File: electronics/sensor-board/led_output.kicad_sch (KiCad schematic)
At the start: 0 parts

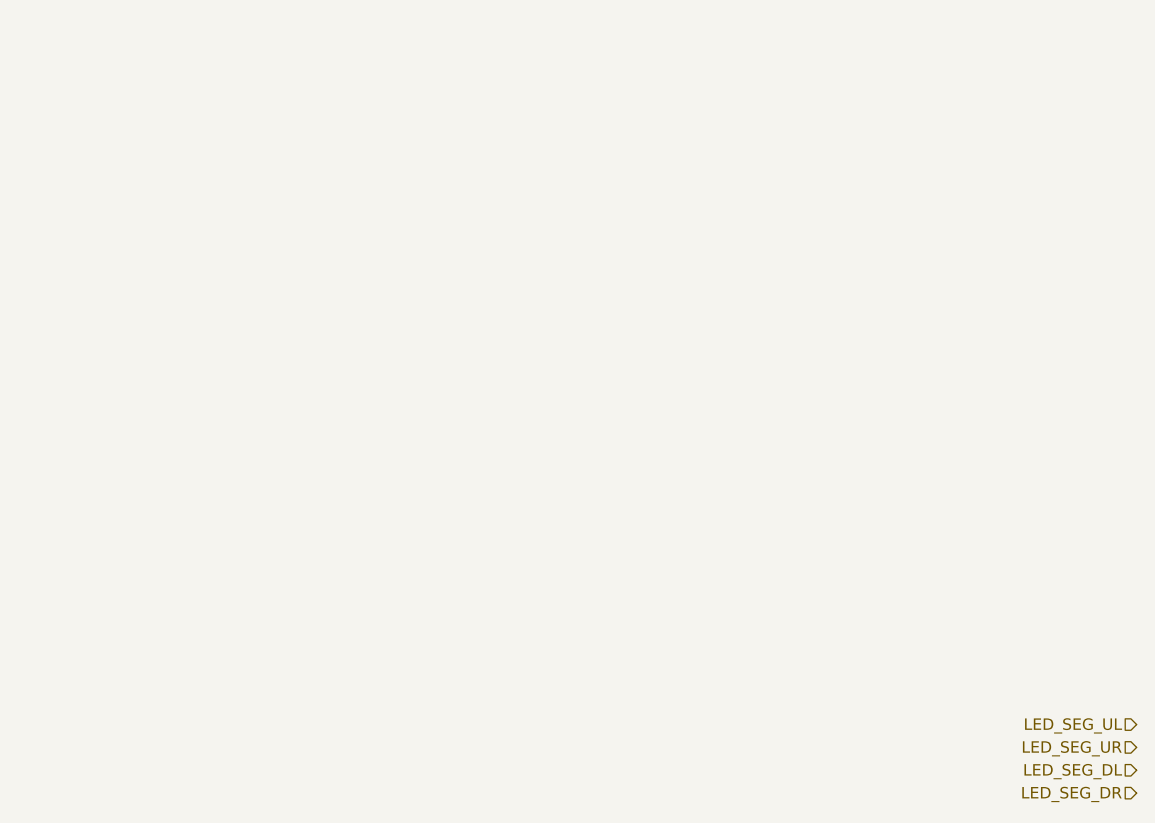
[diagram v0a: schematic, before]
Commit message: LED output, debug and minor controller changes
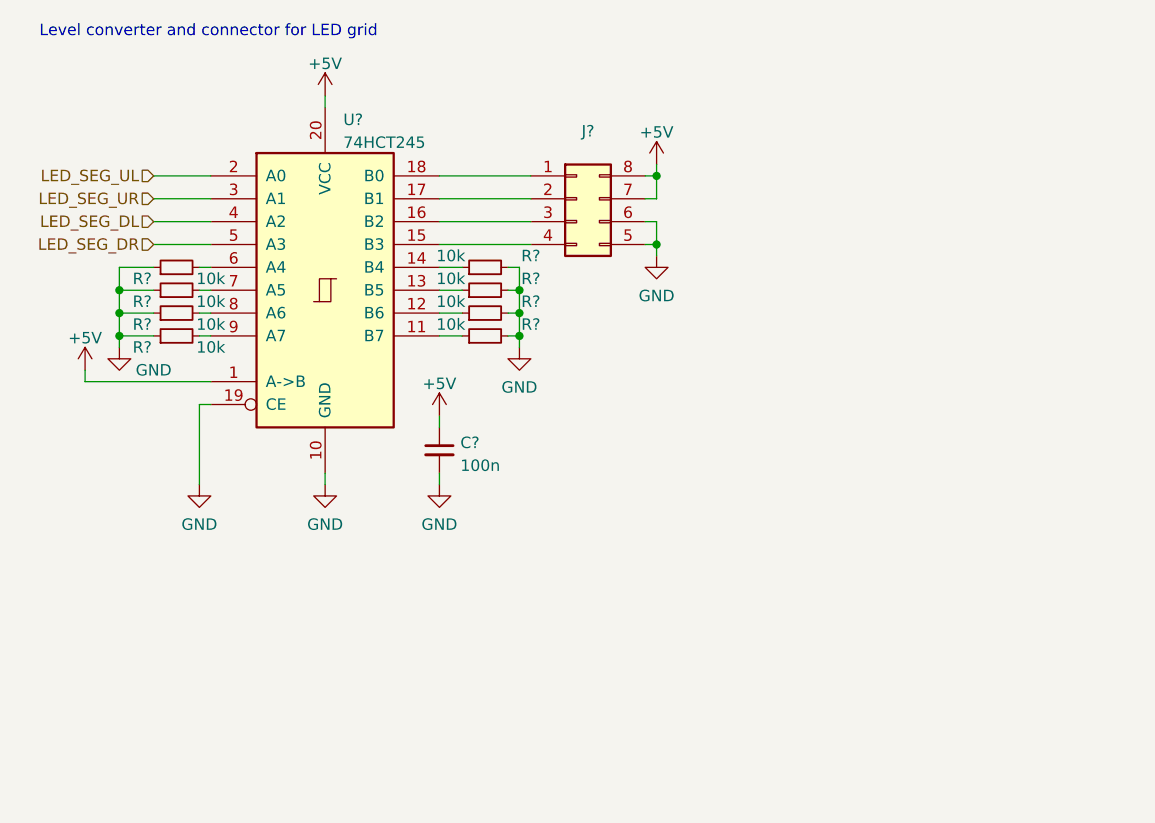
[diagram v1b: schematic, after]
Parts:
- added C?: 100n, symbol Device:C_Small
- added J?: Conn_02x04_Counter_Clockwise, symbol Connector_Generic:Conn_02x04_Counter_Clockwise
- added R? (x8): 10k, symbol Device:R_Small
- added U?: 74HCT245, symbol 74xx:74HC245
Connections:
- net LED_SEG_DL: now also U?.4 (A2)
- net LED_SEG_DR: now also U?.5 (A3)
- net LED_SEG_UL: now also U?.2 (A0)
- net LED_SEG_UR: now also U?.3 (A1)
- new net: R?.2, U?.6 (A4)
- new net: R?.1, U?.14 (B4)
- new net: R?.1, U?.12 (B6)
- new net: J?.1 (Pin_1), U?.18 (B0)
- new net: J?.2 (Pin_2), U?.17 (B1)
- new net: J?.3 (Pin_3), U?.16 (B2)
- new net: J?.4 (Pin_4), U?.15 (B3)
- new net: R?.1, U?.13 (B5)
- new net: R?.1, U?.11 (B7)
- new net: R?.2, U?.7 (A5)
- new net: R?.2, U?.8 (A6)
- new net: R?.2, U?.9 (A7)
- new net +5V: C?.1, J?.7 (Pin_7), J?.8 (Pin_8), U?.1 (A->B), U?.20 (VCC)
- new net GND: C?.2, J?.5 (Pin_5), J?.6 (Pin_6), R?.1, R?.1, R?.1, R?.1, R?.2, R?.2, R?.2, R?.2, U?.10 (GND), U?.19 (CE)
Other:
- note added: "Level converter and connector for LED grid"

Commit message: Build Pad Bus and annotate
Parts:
- gave numbers to parts that had none: 11
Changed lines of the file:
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@@
   (symbol (lib_id "Device:R_Small") (at 33.02 41.91 90) (unit 1)
     (in_bom yes) (on_board yes)
-    (property "Reference" "R?" (id 0) (at 29.21 43.18 90))
+    (property "Reference" "R59" (id 0) (at 29.21 43.18 90))
     (property "Value" "10k" (id 1) (at 36.83 43.18 90))
     (property "Footprint" "" (id 2) (at 33.02 41.91 0)
@@
   (symbol (lib_id "Device:R_Small") (at 67.31 41.91 90) (unit 1)
     (in_bom yes) (on_board yes)
-    (property "Reference" "R?" (id 0) (at 72.39 40.64 90))
+    (property "Reference" "R63" (id 0) (at 73.66 40.64 90))
     (property "Value" "10k" (id 1) (at 63.5 40.64 90))
     (property "Footprint" "" (id 2) (at 67.31 41.91 0)
@@
   (symbol (lib_id "power:GND") (at 49.53 66.04 0) (unit 1)
     (in_bom yes) (on_board yes) (fields_autoplaced)
-    (property "Reference" "#PWR?" (id 0) (at 49.53 72.39 0)
+    (property "Reference" "#PWR0108" (id 0) (at 49.53 72.39 0)
       (effects (font (size 1.27 1.27)) hide)
     )
@@
   (symbol (lib_id "power:GND") (at 62.23 66.04 0) (unit 1)
     (in_bom yes) (on_board yes) (fields_autoplaced)
-    (property "Reference" "#PWR?" (id 0) (at 62.23 72.39 0)
+    (property "Reference" "#PWR0110" (id 0) (at 62.23 72.39 0)
       (effects (font (size 1.27 1.27)) hide)
     )
@@
   (symbol (lib_id "Device:R_Small") (at 67.31 46.99 90) (unit 1)
     (in_bom yes) (on_board yes)
-    (property "Reference" "R?" (id 0) (at 72.39 45.72 90))
+    (property "Reference" "R65" (id 0) (at 73.66 45.72 90))
     (property "Value" "10k" (id 1) (at 63.5 45.72 90))
     (property "Footprint" "" (id 2) (at 67.31 46.99 0)
@@
   (symbol (lib_id "power:GND") (at 26.67 50.8 0) (unit 1)
     (in_bom yes) (on_board yes)
-    (property "Reference" "#PWR?" (id 0) (at 26.67 57.15 0)
+    (property "Reference" "#PWR0105" (id 0) (at 26.67 57.15 0)
       (effects (font (size 1.27 1.27)) hide)
     )
@@
   (symbol (lib_id "power:+5V") (at 62.23 58.42 0) (unit 1)
     (in_bom yes) (on_board yes) (fields_autoplaced)
-    (property "Reference" "#PWR?" (id 0) (at 62.23 62.23 0)
+    (property "Reference" "#PWR0109" (id 0) (at 62.23 62.23 0)
       (effects (font (size 1.27 1.27)) hide)
     )
@@
   (symbol (lib_id "power:GND") (at 71.12 50.8 0) (unit 1)
     (in_bom yes) (on_board yes) (fields_autoplaced)
-    (property "Reference" "#PWR?" (id 0) (at 71.12 57.15 0)
+    (property "Reference" "#PWR0111" (id 0) (at 71.12 57.15 0)
       (effects (font (size 1.27 1.27)) hide)
     )
@@
   (symbol (lib_id "power:+5V") (at 22.86 53.34 0) (unit 1)
     (in_bom yes) (on_board yes) (fields_autoplaced)
-    (property "Reference" "#PWR?" (id 0) (at 22.86 57.15 0)
+    (property "Reference" "#PWR0104" (id 0) (at 22.86 57.15 0)
       (effects (font (size 1.27 1.27)) hide)
     )
@@
   (symbol (lib_id "Connector_Generic:Conn_02x04_Counter_Clockwise") (at 77.47 34.29 0) (unit 1)
     (in_bom yes) (on_board yes) (fields_autoplaced)
-    (property "Reference" "J?" (id 0) (at 78.74 26.7802 0))
+    (property "Reference" "J19" (id 0) (at 78.74 26.7802 0))
     (property "Value" "Conn_02x04_Counter_Clockwise" (id 1) (at 78.74 29.3171 0)
       (effects (font (size 1.27 1.27)) hide)
@@
   (symbol (lib_id "Device:R_Small") (at 67.31 44.45 90) (unit 1)
     (in_bom yes) (on_board yes)
-    (property "Reference" "R?" (id 0) (at 72.39 43.18 90))
+    (property "Reference" "R64" (id 0) (at 73.66 43.18 90))
     (property "Value" "10k" (id 1) (at 63.5 43.18 90))
     (property "Footprint" "" (id 2) (at 67.31 44.45 0)
@@
   (symbol (lib_id "74xx:74HC245") (at 49.53 44.45 0) (unit 1)
     (in_bom yes) (on_board yes) (fields_autoplaced)
-    (property "Reference" "U?" (id 0) (at 51.5494 25.5102 0)
+    (property "Reference" "U11" (id 0) (at 51.5494 25.5102 0)
       (effects (font (size 1.27 1.27)) (justify left))
     )
@@
   (symbol (lib_id "Device:R_Small") (at 33.02 49.53 90) (unit 1)
     (in_bom yes) (on_board yes)
-    (property "Reference" "R?" (id 0) (at 29.21 50.8 90))
+    (property "Reference" "R62" (id 0) (at 29.21 50.8 90))
     (property "Value" "10k" (id 1) (at 36.83 50.8 90))
     (property "Footprint" "" (id 2) (at 33.02 49.53 0)
@@
   (symbol (lib_id "power:GND") (at 86.36 40.64 0) (unit 1)
     (in_bom yes) (on_board yes) (fields_autoplaced)
-    (property "Reference" "#PWR?" (id 0) (at 86.36 46.99 0)
+    (property "Reference" "#PWR0113" (id 0) (at 86.36 46.99 0)
       (effects (font (size 1.27 1.27)) hide)
     )
@@
   (symbol (lib_id "power:GND") (at 35.56 66.04 0) (unit 1)
     (in_bom yes) (on_board yes) (fields_autoplaced)
-    (property "Reference" "#PWR?" (id 0) (at 35.56 72.39 0)
+    (property "Reference" "#PWR0106" (id 0) (at 35.56 72.39 0)
       (effects (font (size 1.27 1.27)) hide)
     )
@@
   (symbol (lib_id "power:+5V") (at 49.53 22.86 0) (unit 1)
     (in_bom yes) (on_board yes) (fields_autoplaced)
-    (property "Reference" "#PWR?" (id 0) (at 49.53 26.67 0)
+    (property "Reference" "#PWR0107" (id 0) (at 49.53 26.67 0)
       (effects (font (size 1.27 1.27)) hide)
     )
@@
   (symbol (lib_id "Device:R_Small") (at 33.02 46.99 90) (unit 1)
     (in_bom yes) (on_board yes)
-    (property "Reference" "R?" (id 0) (at 29.21 48.26 90))
+    (property "Reference" "R61" (id 0) (at 29.21 48.26 90))
     (property "Value" "10k" (id 1) (at 36.83 48.26 90))
     (property "Footprint" "" (id 2) (at 33.02 46.99 0)
@@
   (symbol (lib_id "Device:R_Small") (at 67.31 49.53 90) (unit 1)
     (in_bom yes) (on_board yes)
-    (property "Reference" "R?" (id 0) (at 72.39 48.26 90))
+    (property "Reference" "R66" (id 0) (at 73.66 48.26 90))
     (property "Value" "10k" (id 1) (at 63.5 48.26 90))
     (property "Footprint" "" (id 2) (at 67.31 49.53 0)
@@
   (symbol (lib_id "Device:C_Small") (at 62.23 62.23 0) (unit 1)
     (in_bom yes) (on_board yes) (fields_autoplaced)
-    (property "Reference" "C?" (id 0) (at 64.5541 61.4016 0)
+    (property "Reference" "C46" (id 0) (at 64.5541 61.4016 0)
       (effects (font (size 1.27 1.27)) (justify left))
     )
@@
   (symbol (lib_id "Device:R_Small") (at 33.02 44.45 90) (unit 1)
     (in_bom yes) (on_board yes)
-    (property "Reference" "R?" (id 0) (at 29.21 45.72 90))
+    (property "Reference" "R60" (id 0) (at 29.21 45.72 90))
     (property "Value" "10k" (id 1) (at 36.83 45.72 90))
     (property "Footprint" "" (id 2) (at 33.02 44.45 0)
@@
   (symbol (lib_id "power:+5V") (at 86.36 30.48 0) (unit 1)
     (in_bom yes) (on_board yes) (fields_autoplaced)
-    (property "Reference" "#PWR?" (id 0) (at 86.36 34.29 0)
-      (effects (font (size 1.27 1.27)) hide)
-    )
+    (property "Reference" "#PWR0112" (id 0) (at 86.36 34.29 0)
+      (effects (font (size 1.27 1.27)) hide)
+    )

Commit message: Minor tweaks, footprints added
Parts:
- C46: footprint (none) -> Capacitor_SMD:C_0603_1608Metric
- J19: footprint (none) -> Connector_PinHeader_2.54mm:PinHeader_2x04_P2.54mm_Vertical
- R59, R60, R61, R62, R63, R64, R65, R66: footprint (none) -> Resistor_SMD:R_0603_1608Metric
- U11: footprint (none) -> Package_SO:TSSOP-20_4.4x6.5mm_P0.65mm
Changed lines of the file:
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@@
     (property "Reference" "R59" (id 0) (at 29.21 43.18 90))
     (property "Value" "10k" (id 1) (at 36.83 43.18 90))
-    (property "Footprint" "" (id 2) (at 33.02 41.91 0)
+    (property "Footprint" "Resistor_SMD:R_0603_1608Metric" (id 2) (at 33.02 41.91 0)
       (effects (font (size 1.27 1.27)) hide)
     )
@@
     (property "Reference" "R63" (id 0) (at 73.66 40.64 90))
     (property "Value" "10k" (id 1) (at 63.5 40.64 90))
-    (property "Footprint" "" (id 2) (at 67.31 41.91 0)
+    (property "Footprint" "Resistor_SMD:R_0603_1608Metric" (id 2) (at 67.31 41.91 0)
       (effects (font (size 1.27 1.27)) hide)
     )
@@
     (property "Reference" "R65" (id 0) (at 73.66 45.72 90))
     (property "Value" "10k" (id 1) (at 63.5 45.72 90))
-    (property "Footprint" "" (id 2) (at 67.31 46.99 0)
+    (property "Footprint" "Resistor_SMD:R_0603_1608Metric" (id 2) (at 67.31 46.99 0)
       (effects (font (size 1.27 1.27)) hide)
     )
@@
       (effects (font (size 1.27 1.27)) hide)
     )
-    (property "Footprint" "" (id 2) (at 77.47 34.29 0)
+    (property "Footprint" "Connector_PinHeader_2.54mm:PinHeader_2x04_P2.54mm_Vertical" (id 2) (at 77.47 34.29 0)
       (effects (font (size 1.27 1.27)) hide)
     )
@@
     (property "Reference" "R64" (id 0) (at 73.66 43.18 90))
     (property "Value" "10k" (id 1) (at 63.5 43.18 90))
-    (property "Footprint" "" (id 2) (at 67.31 44.45 0)
+    (property "Footprint" "Resistor_SMD:R_0603_1608Metric" (id 2) (at 67.31 44.45 0)
       (effects (font (size 1.27 1.27)) hide)
     )
@@
       (effects (font (size 1.27 1.27)) (justify left))
     )
-    (property "Footprint" "" (id 2) (at 49.53 44.45 0)
+    (property "Footprint" "Package_SO:TSSOP-20_4.4x6.5mm_P0.65mm" (id 2) (at 49.53 44.45 0)
       (effects (font (size 1.27 1.27)) hide)
     )
@@
     (property "Reference" "R62" (id 0) (at 29.21 50.8 90))
     (property "Value" "10k" (id 1) (at 36.83 50.8 90))
-    (property "Footprint" "" (id 2) (at 33.02 49.53 0)
+    (property "Footprint" "Resistor_SMD:R_0603_1608Metric" (id 2) (at 33.02 49.53 0)
       (effects (font (size 1.27 1.27)) hide)
     )
@@
     (property "Reference" "R61" (id 0) (at 29.21 48.26 90))
     (property "Value" "10k" (id 1) (at 36.83 48.26 90))
-    (property "Footprint" "" (id 2) (at 33.02 46.99 0)
+    (property "Footprint" "Resistor_SMD:R_0603_1608Metric" (id 2) (at 33.02 46.99 0)
       (effects (font (size 1.27 1.27)) hide)
     )
@@
     (property "Reference" "R66" (id 0) (at 73.66 48.26 90))
     (property "Value" "10k" (id 1) (at 63.5 48.26 90))
-    (property "Footprint" "" (id 2) (at 67.31 49.53 0)
+    (property "Footprint" "Resistor_SMD:R_0603_1608Metric" (id 2) (at 67.31 49.53 0)
       (effects (font (size 1.27 1.27)) hide)
     )
@@
       (effects (font (size 1.27 1.27)) (justify left))
     )
-    (property "Footprint" "" (id 2) (at 62.23 62.23 0)
+    (property "Footprint" "Capacitor_SMD:C_0603_1608Metric" (id 2) (at 62.23 62.23 0)
       (effects (font (size 1.27 1.27)) hide)
     )
@@
     (property "Reference" "R60" (id 0) (at 29.21 45.72 90))
     (property "Value" "10k" (id 1) (at 36.83 45.72 90))
-    (property "Footprint" "" (id 2) (at 33.02 44.45 0)
-      (effects (font (size 1.27 1.27)) hide)
-    )
+    (property "Footprint" "Resistor_SMD:R_0603_1608Metric" (id 2) (at 33.02 44.45 0)
+      (effects (font (size 1.27 1.27)) hide)
+    )

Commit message: Final tweaks and schematic review complete
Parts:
- removed J19: Conn_02x04_Counter_Clockwise, Connector_PinHeader_2.54mm:PinHeader_2x04_P2.54mm_Vertical, symbol Connector_Generic:Conn_02x04_Counter_Clockwise
- added J19: Conn_02x04_Odd_Even, Connector_PinHeader_2.54mm:PinHeader_2x04_P2.54mm_Vertical, symbol Connector_Generic:Conn_02x04_Odd_Even
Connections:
- net +5V: now also J19.2 (Pin_2), J19.4 (Pin_4)
- net GND: now also J19.6 (Pin_6), J19.8 (Pin_8)
- net at U11.18 (B0): now also J19.1 (Pin_1)
- net at U11.17 (B1): now also J19.3 (Pin_3)
- net at U11.16 (B2): now also J19.5 (Pin_5)
- net at U11.15 (B3): now also J19.7 (Pin_7)
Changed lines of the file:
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@@
     (pin "1")
-  )
-  (symbol (lib_id "Connector_Generic:Conn_02x04_Counter_Clockwise") (at 77.47 34.29 0) (unit 1)
-    (in_bom yes) (on_board yes) (fields_autoplaced)
-    (property "Reference" "J19" (id 0) (at 78.74 26.7802 0))
-    (property "Value" "Conn_02x04_Counter_Clockwise" (id 1) (at 78.74 29.3171 0)
-      (effects (font (size 1.27 1.27)) hide)
-    )
-    (property "Footprint" "Connector_PinHeader_2.54mm:PinHeader_2x04_P2.54mm_Vertical" (id 2) (at 77.47 34.29 0)
-      (effects (font (size 1.27 1.27)) hide)
-    )
-    (property "Datasheet" "~" (id 3) (at 77.47 34.29 0)
-      (effects (font (size 1.27 1.27)) hide)
-    )
-    (pin "1")
-    (pin "2")
-    (pin "3")
-    (pin "4")
-    (pin "5")
-    (pin "6")
-    (pin "7")
-    (pin "8")
   )
   (symbol (lib_id "Device:R_Small") (at 67.31 44.45 90) (unit 1)
@@
     (pin "2")
   )
+  (symbol (lib_id "Connector_Generic:Conn_02x04_Odd_Even") (at 77.47 34.29 0) (unit 1)
+    (in_bom yes) (on_board yes) (fields_autoplaced)
+    (property "Reference" "J19" (id 0) (at 78.74 26.7802 0))
+    (property "Value" "Conn_02x04_Odd_Even" (id 1) (at 78.74 29.3171 0)
+      (effects (font (size 1.27 1.27)) hide)
+    )
+    (property "Footprint" "Connector_PinHeader_2.54mm:PinHeader_2x04_P2.54mm_Vertical" (id 2) (at 77.47 34.29 0)
+      (effects (font (size 1.27 1.27)) hide)
+    )
+    (property "Datasheet" "~" (id 3) (at 77.47 34.29 0)
+      (effects (font (size 1.27 1.27)) hide)
+    )
+    (pin "1")
+    (pin "2")
+    (pin "3")
+    (pin "4")
+    (pin "5")
+    (pin "6")
+    (pin "7")
+    (pin "8")
+  )
   (symbol (lib_id "Device:C_Small") (at 62.23 62.23 0) (unit 1)

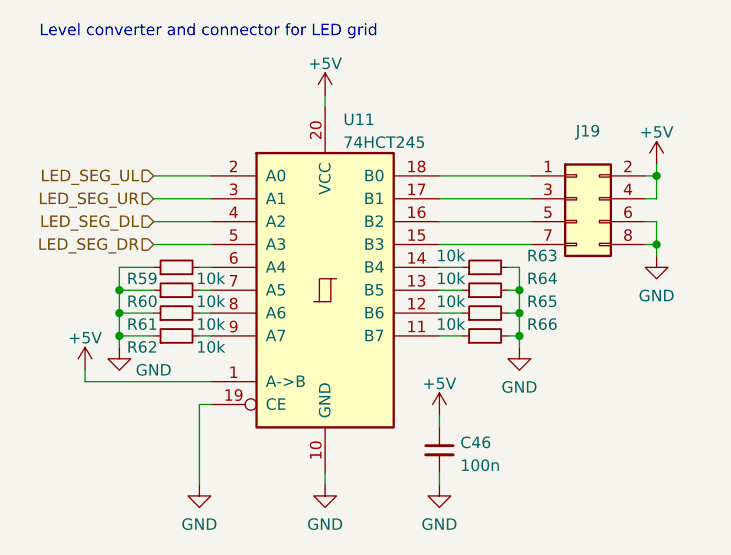
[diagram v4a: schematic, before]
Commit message: Remove DIP switches and re-organize CAN connectors
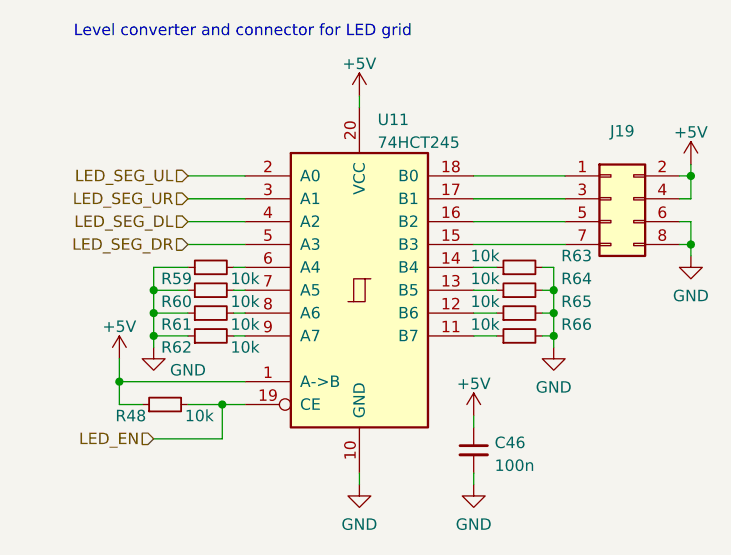
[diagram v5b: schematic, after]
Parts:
- added R48: 10k, Resistor_SMD:R_0603_1608Metric, symbol Device:R_Small
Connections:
- net +5V: now also R48.1
- net GND: no longer U11.19 (CE)
- new net LED_EN: R48.2, U11.19 (CE)
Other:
- moved on the sheet: C46, J19, R59, R60, R61, R62, R63, R64, R65, R66, U11
